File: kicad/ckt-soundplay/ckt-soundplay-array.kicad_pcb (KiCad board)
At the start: 2 copper layers, 91.4 x 176.5 mm, 269 parts, among them J1 Screw_Terminal_01x02, J10 SM04B-SRSS, J2 Screw_Terminal_01x02, J3 Screw_Terminal_01x02, J4 Screw_Terminal_01x02, J5 690-005-299-043, J6 SM04B-SRSS, J7 Micro_SD_Card_Det_Hirose_DM3AT, J8 Screw_Terminal_01x02, J9 Conn_01x05, SW1 FSM4JSMATR, SW2 FSM4JSMATR, U1 AP63203WU, U2 ESP32-S2-SOLO, U3 MAX98357AETE+T

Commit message: Update to 1.3 instead of 1.2A because Michael
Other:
- board text added: "Iowa Scaled Engineering CKT-SOUNDPLAY v1.3 ©2026 CC BY-SA"
- board text removed: "Iowa Scaled Engineering CKT-SOUNDPLAY v1.2A ©2026 CC BY-SA"

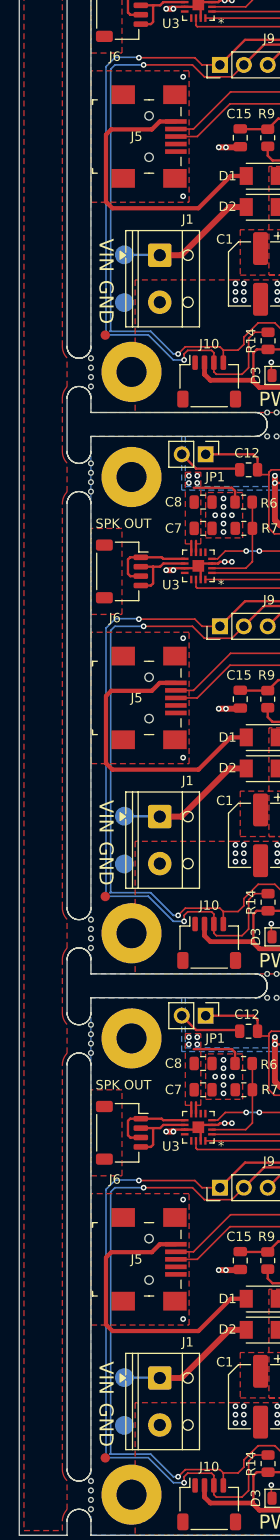
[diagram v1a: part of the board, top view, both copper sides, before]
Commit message: Update footprint, recreate panel
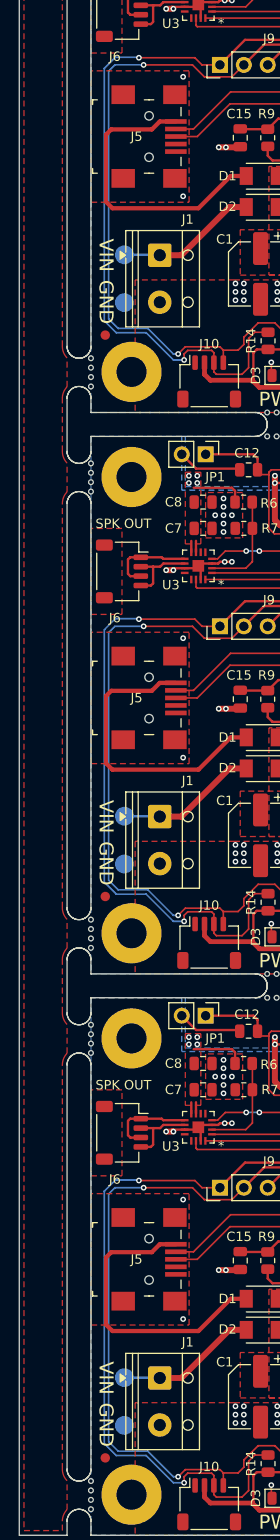
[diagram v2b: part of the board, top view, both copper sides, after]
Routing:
- net Board_1-/AUX2: track 80.7 -> 80.1 mm
- net Board_2-/AUX2: track 80.7 -> 80.1 mm
- net Board_0-/AUX2: track 80.7 -> 80.1 mm

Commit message: Update panel - new QFN, move fiducial
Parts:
- removed KiKit_MB_14_1, KiKit_MB_14_2, KiKit_MB_14_3, KiKit_MB_14_4, KiKit_MB_15_1, KiKit_MB_15_2, KiKit_MB_15_3, KiKit_MB_15_4, KiKit_MB_16_1, KiKit_MB_16_2, KiKit_MB_16_3, KiKit_MB_16_4, KiKit_MB_17_1, KiKit_MB_17_2, KiKit_MB_17_3, KiKit_MB_17_4: NPTH, NPTH
- removed the U3 at (121.8, 153.1)
- removed the U3 at (121.8, 93.5)
- removed the U3 at (121.8, 33.8)
- added U3: MAX98357AETE+T, Package_DFN_QFN:TQFN-16-1EP_3x3mm_P0.5mm_EP1.23x1.23mm, F.Cu at (121.8, 153.1)
- added U3: MAX98357AETE+T, Package_DFN_QFN:TQFN-16-1EP_3x3mm_P0.5mm_EP1.23x1.23mm, F.Cu at (121.8, 93.5)
- added U3: MAX98357AETE+T, Package_DFN_QFN:TQFN-16-1EP_3x3mm_P0.5mm_EP1.23x1.23mm, F.Cu at (121.8, 33.8)
- moved KiKit_MB_12_1 108.2 mm to (110.4, 193.8)
- moved KiKit_MB_12_2 108.2 mm to (110.4, 192.8)
- moved KiKit_MB_12_3 108.2 mm to (110.4, 191.8)
- moved KiKit_MB_12_4 108.2 mm to (110.4, 190.8)
- moved KiKit_MB_5_4 77.1 mm to (162.5, 79.7)
- moved KiKit_MB_5_3 75.7 mm to (161.5, 79.7)
- moved KiKit_MB_5_2 74.3 mm to (160.5, 79.7)
- moved KiKit_MB_5_1 72.9 mm to (159.5, 79.7)
- moved KiKit_MB_13_4 71.2 mm to (110.4, 142.2)
- moved KiKit_MB_8_1 71.2 mm to (110.4, 134.1)
- moved KiKit_MB_13_3 70.3 mm to (110.4, 143.2)
- moved KiKit_MB_8_2 70.2 mm to (110.4, 133.1)
- moved KiKit_MB_13_2 69.3 mm to (110.4, 144.2)
- moved KiKit_MB_8_3 69.3 mm to (110.4, 132.1)
- moved KiKit_MB_13_1 68.4 mm to (110.4, 145.2)
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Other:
- outline, holes or cut-outs redrawn
